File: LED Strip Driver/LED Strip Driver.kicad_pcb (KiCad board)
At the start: 2 copper layers, 33.6 x 16.9 mm, 10 parts, among them J1 Screw_Terminal_01x02, J2 Conn_01x02_Pin, J3 Screw_Terminal_01x02, U1 TPS92360

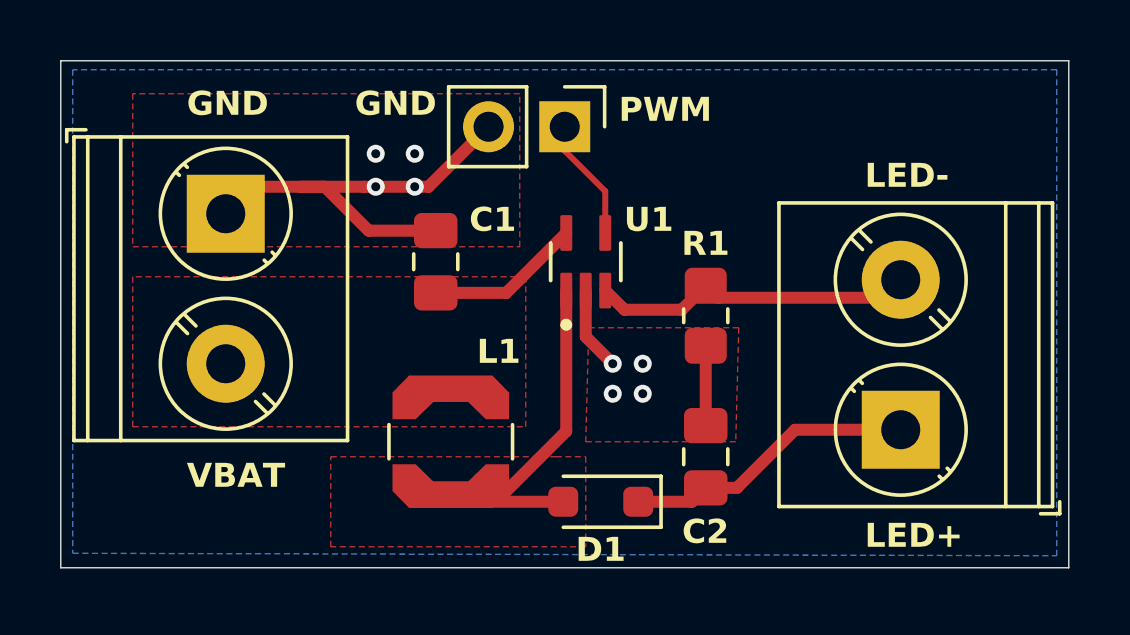
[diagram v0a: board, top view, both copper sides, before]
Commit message: flip pwm connector so gnd pad is square
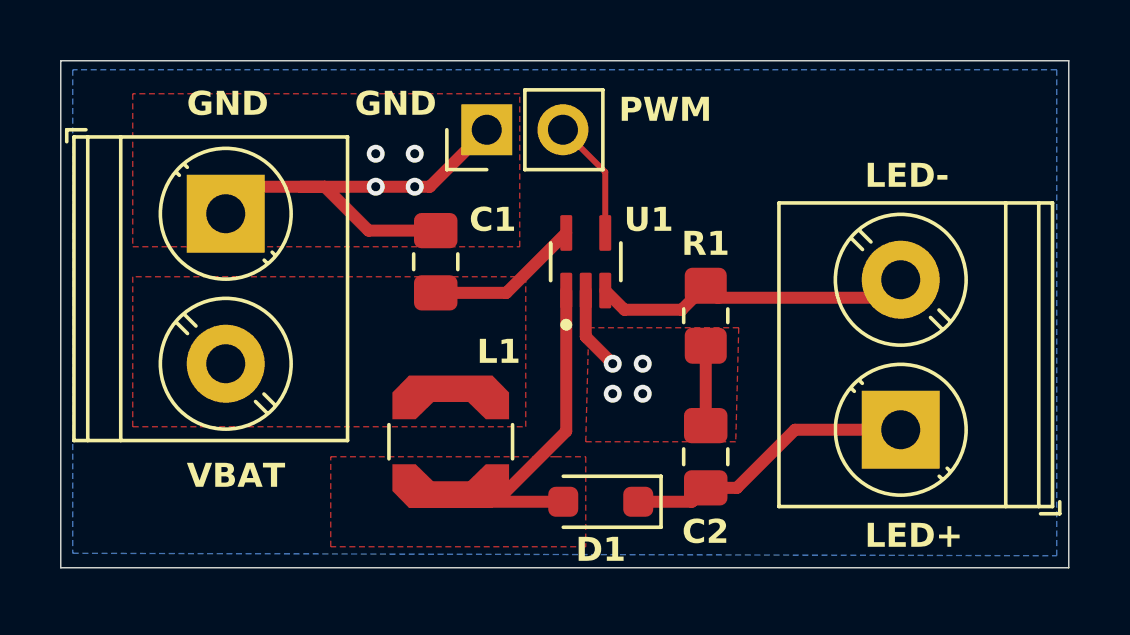
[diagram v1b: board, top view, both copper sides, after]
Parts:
- moved J2 2.60 mm to (153.2, 80.6), turned to 90 degrees
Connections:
- J2 pad 1: /PWM_CTRL -> GND
- J2 pad 2: GND -> /PWM_CTRL
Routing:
- net /PWM_CTRL: track 4.10 -> 4.82 mm
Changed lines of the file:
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@@
 	(footprint "Connector_PinHeader_2.54mm:PinHeader_1x02_P2.54mm_Vertical"
 		(layer "F.Cu")
-		(at 155.8 80.5 -90)
+		(at 153.2 80.6 90)
 		(descr "Through hole straight pin header, 1x02, 2.54mm pitch, single row")
 		(tags "Through hole pin header THT 1x02 2.54mm single row")
 		(property "Reference" "J2"
 			(at 0 -2.33 90)
-			(layer "F.Fab")
+			(layer "B.Fab")
 			(effects
 				(font
@@
 					(thickness 0.15)
 				)
+				(justify mirror)
 			)
 		)
 		(property "Value" "Conn_01x02_Pin"
 			(at 0 4.87 90)
-			(layer "F.Fab")
+			(layer "B.Fab")
 			(effects
 				(font
@@
 					(thickness 0.15)
 				)
+				(justify mirror)
 			)
 		)
 		(property "Footprint" "Connector_PinHeader_2.54mm:PinHeader_1x02_P2.54mm_Vertical"
-			(at 0 0 -90)
+			(at 0 0 90)
 			(unlocked yes)
-			(layer "F.Fab")
+			(layer "B.Fab")
 			(hide yes)
 			(effects
@@
 					(thickness 0.15)
 				)
+				(justify mirror)
 			)
 		)
 		(property "Datasheet" ""
-			(at 0 0 -90)
+			(at 0 0 90)
 			(unlocked yes)
-			(layer "F.Fab")
+			(layer "B.Fab")
 			(hide yes)
 			(effects
@@
 					(thickness 0.15)
 				)
+				(justify mirror)
 			)
 		)
 		(property "Description" "Generic connector, single row, 01x02, script generated"
-			(at 0 0 -90)
+			(at 0 0 90)
 			(unlocked yes)
-			(layer "F.Fab")
+			(layer "B.Fab")
 			(hide yes)
 			(effects
@@
 					(thickness 0.15)
 				)
+				(justify mirror)
 			)
 		)
@@
 		(attr through_hole)
 		(fp_line
-			(start -1.33 3.87)
-			(end 1.33 3.87)
+			(start -1.33 -1.33)
+			(end 0 -1.33)
 			(stroke
 				(width 0.12)
@@
 		)
 		(fp_line
-			(start -1.33 1.27)
-			(end -1.33 3.87)
+			(start -1.33 0)
+			(end -1.33 -1.33)
 			(stroke
 				(width 0.12)
@@
 		)
 		(fp_line
-			(start -1.33 1.27)
-			(end 1.33 1.27)
+			(start 1.33 1.27)
+			(end 1.33 3.87)
 			(stroke
 				(width 0.12)
@@
 		)
 		(fp_line
-			(start 1.33 1.27)
-			(end 1.33 3.87)
+			(start -1.33 1.27)
+			(end 1.33 1.27)
 			(stroke
 				(width 0.12)
@@
 		)
 		(fp_line
-			(start -1.33 0)
-			(end -1.33 -1.33)
+			(start -1.33 1.27)
+			(end -1.33 3.87)
 			(stroke
 				(width 0.12)
@@
 		)
 		(fp_line
-			(start -1.33 -1.33)
-			(end 0 -1.33)
+			(start -1.33 3.87)
+			(end 1.33 3.87)
 			(stroke
 				(width 0.12)
@@
 		)
 		(fp_line
-			(start -1.8 4.35)
-			(end 1.8 4.35)
+			(start 1.8 -1.8)
+			(end -1.8 -1.8)
 			(stroke
 				(width 0.05)
@@
 		)
 		(fp_line
-			(start 1.8 4.35)
-			(end 1.8 -1.8)
+			(start -1.8 -1.8)
+			(end -1.8 4.35)
 			(stroke
 				(width 0.05)
@@
 		)
 		(fp_line
-			(start -1.8 -1.8)
-			(end -1.8 4.35)
+			(start 1.8 4.35)
+			(end 1.8 -1.8)
 			(stroke
 				(width 0.05)
@@
 		)
 		(fp_line
-			(start 1.8 -1.8)
-			(end -1.8 -1.8)
+			(start -1.8 4.35)
+			(end 1.8 4.35)
 			(stroke
 				(width 0.05)
@@
 		)
 		(fp_line
-			(start -1.27 3.81)
-			(end -1.27 -0.635)
+			(start 1.27 -1.27)
+			(end 1.27 3.81)
 			(stroke
 				(width 0.1)
@@
 		)
 		(fp_line
-			(start 1.27 3.81)
-			(end -1.27 3.81)
+			(start -0.635 -1.27)
+			(end 1.27 -1.27)
 			(stroke
 				(width 0.1)
@@
 		)
 		(fp_line
-			(start -0.635 -1.27)
-			(end 1.27 -1.27)
+			(start 1.27 3.81)
+			(end -1.27 3.81)
 			(stroke
 				(width 0.1)
@@
 		)
 		(fp_line
-			(start 1.27 -1.27)
-			(end 1.27 3.81)
+			(start -1.27 3.81)
+			(end -1.27 -0.635)
 			(stroke
 				(width 0.1)
@@
 		)
 		(fp_text user "${REFERENCE}"
-			(at 0 1.27 0)
+			(at 0 1.27 360)
 			(layer "F.Fab")
 			(effects
@@
 		)
 		(pad "1" thru_hole rect
-			(at 0 0 270)
+			(at 0 0 90)
 			(size 1.7 1.7)
 			(drill 1)
 			(layers "*.Cu" "*.Mask")
 			(remove_unused_layers no)
-			(net 6 "/PWM_CTRL")
+			(net 1 "GND")
 			(pinfunction "Pin_1")
 			(pintype "passive")
 		)
 		(pad "2" thru_hole oval
-			(at 0 2.54 270)
+			(at 0 2.54 90)
 			(size 1.7 1.7)
 			(drill 1)
 			(layers "*.Cu" "*.Mask")
 			(remove_unused_layers no)
-			(net 1 "GND")
+			(net 6 "/PWM_CTRL")
 			(pinfunction "Pin_2")
 			(pintype "passive")
@@
 	)
 	(segment
-		(start 149.1 82.5)
-		(end 145.4 82.5)
-		(width 0.4)
-		(layer "F.Cu")
-		(net 1)
-	)
-	(segment
-		(start 149.1 82.5)
-		(end 151.26 82.5)
+		(start 156.5 87.5)
+		(end 156.5 85.96)
 		(width 0.4)
 		(layer "F.Cu")
@@
 	)
 	(segment
-		(start 156.5 87.5)
-		(end 156.5 85.96)
+		(start 157.4 88.4)
+		(end 156.5 87.5)
 		(width 0.4)
 		(layer "F.Cu")
@@
 	)
 	(segment
-		(start 151.26 82.5)
-		(end 153.26 80.5)
+		(start 147.8 82.5)
+		(end 147 82.5)
 		(width 0.4)
 		(layer "F.Cu")
@@
 	)
 	(segment
-		(start 157.4 88.4)
-		(end 156.5 87.5)
+		(start 147.8 82.5)
+		(end 149.2625 83.9625)
 		(width 0.4)
 		(layer "F.Cu")
@@
 	)
 	(segment
-		(start 147.8 82.5)
-		(end 147 82.5)
+		(start 153.2 80.6)
+		(end 151.3 82.5)
 		(width 0.4)
 		(layer "F.Cu")
@@
 	)
 	(segment
-		(start 147.8 82.5)
-		(end 149.2625 83.9625)
+		(start 145.4 82.5)
+		(end 144.5 83.4)
 		(width 0.4)
 		(layer "F.Cu")
@@
 	)
 	(segment
-		(start 145.4 82.5)
-		(end 144.5 83.4)
+		(start 151.3 82.5)
+		(end 145.4 82.5)
 		(width 0.4)
 		(layer "F.Cu")
@@
 	)
 	(segment
-		(start 157.15 84.04)
-		(end 157.15 82.65)
+		(start 155.74 80.6)
+		(end 157.15 82.01)
 		(width 0.2)
 		(layer "F.Cu")
@@
 	)
 	(segment
-		(start 155.8 81.3)
-		(end 155.8 80.5)
+		(start 157.15 82.01)
+		(end 157.15 84.04)
 		(width 0.2)
 		(layer "F.Cu")
@@
 	)
 	(segment
-		(start 157.15 82.65)
-		(end 155.8 81.3)
+		(start 155.8 81.3)
+		(end 155.8 80.5)
 		(width 0.2)
 		(layer "F.Cu")
